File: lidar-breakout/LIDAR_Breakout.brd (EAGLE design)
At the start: 36.5 x 88 mm, 82 parts

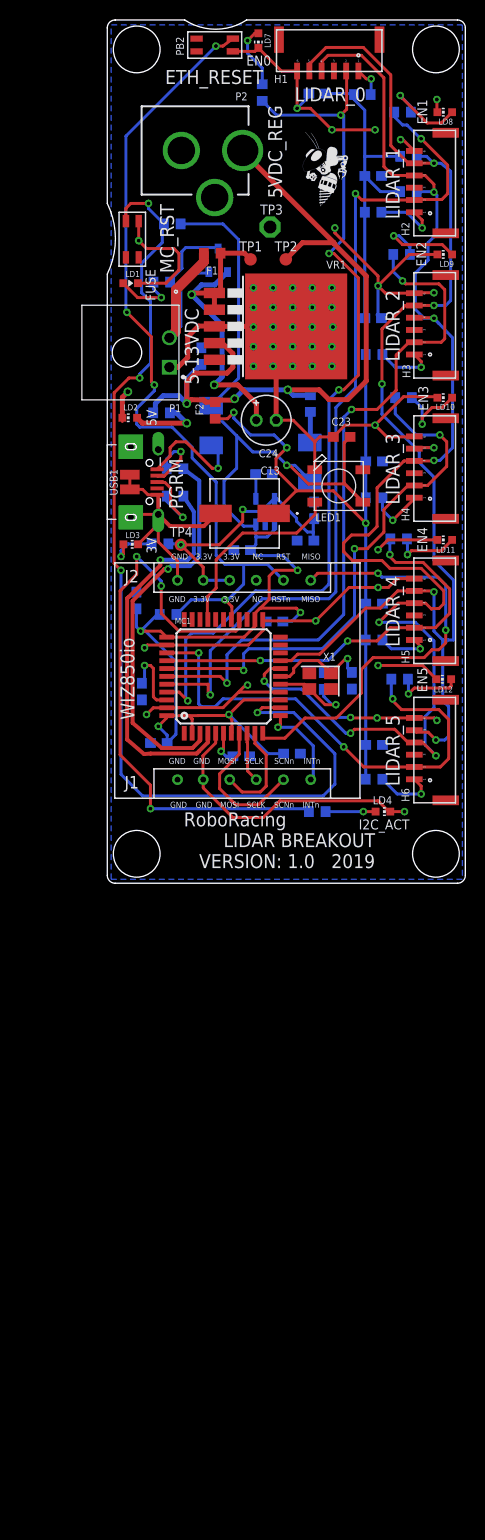
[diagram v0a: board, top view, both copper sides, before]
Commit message: Updated several packages, finished parts list.
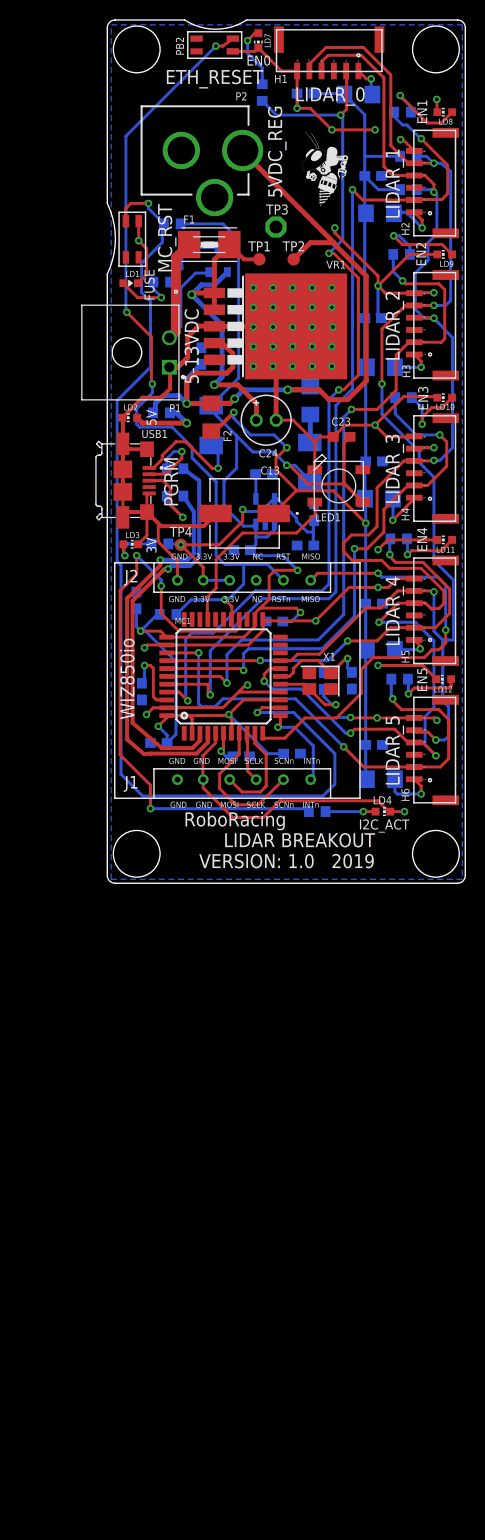
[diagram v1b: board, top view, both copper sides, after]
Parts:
- C3, C4: value 22 pF -> 18 pF
- F1: device RoboJackets-Fuses:F0603 -> adafruit:1812
- F2, F3, F4, F5, F6, F7, F8, F9: device RoboJackets-Fuses:F0603 -> adafruit:R1206
- USB1: value (none) -> 1981584-1; device microbuilder:4UCONN_20329 -> 1981584-1:TE_1981584-1
- moved USB1 2.71 mm to (1.59, 41.0)
- moved F6 1.48 mm to (27.9, 52.6), turned to 180 degrees
- moved F8 1.22 mm to (27.9, 23.8), turned to 180 degrees
- moved C10 1.20 mm to (20.2, 80.5)
- moved F1 0.92 mm to (10.4, 65.1)
- moved TP1 0.90 mm to (15.5, 63.6)
- moved F2 0.81 mm to (10.6, 47.5), turned to 270 degrees
- moved TP2 0.80 mm to (19.0, 63.6)
- moved F5 0.71 mm to (27.8, 68.3), turned to 180 degrees
- moved F9 0.70 mm to (27.9, 10.6), turned to 180 degrees
- moved TP3 0.60 mm to (17.2, 66.9)
- moved F7 0.51 mm to (27.7, 39.2), turned to 180 degrees
- moved C6 0.50 mm to (20.2, 34.4)
- moved F4 0.40 mm to (25.6, 80.4), turned to 180 degrees
- moved F3 0.30 mm to (20.7, 49.2), turned to 270 degrees
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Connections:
- net 5VREG: now also F2.1, F3.1; no longer F2.2, F3.2
- net GND: now also USB1.10, USB1.11, USB1.5, USB1.6, USB1.7, USB1.8, USB1.9; no longer USB1.BASE@1, USB1.BASE@2, USB1.GND, USB1.SPRT@1, USB1.SPRT@2, USB1.SPRT@3, USB1.SPRT@4
- net N$1: now also USB1.1; no longer USB1.VBUS
- net N$23: now also USB1.3; no longer USB1.D+
- net N$7: now also F3.2; no longer F3.1
- net N$8: now also USB1.2; no longer USB1.D-
- net VCC_1: now also F2.2, F4.1, F5.1, F6.1, F7.1, F8.1, F9.1; no longer F2.1, F4.2, F5.2, F6.2, F7.2, F8.2, F9.2
- net VCC_LDR0: now also F4.2; no longer F4.1
- net VCC_LDR1: now also F5.2; no longer F5.1
- net VCC_LDR2: now also F6.2; no longer F6.1
- net VCC_LDR3: now also F7.2; no longer F7.1
- net VCC_LDR4: now also F8.2; no longer F8.1
- net VCC_LDR5: now also F9.2; no longer F9.1
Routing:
- net GND: track 242.9 -> 254.0 mm, vias 47 -> 46
- net VCC_1: track 107.9 -> 110.1 mm
- net VCC_LDR2: track 6.08 -> 4.27 mm
- net VCC_LDR4: track 5.37 -> 3.77 mm
- net VIN: track 34.3 -> 35.5 mm
- net VCC_LDR1: track 6.74 -> 5.51 mm
- net 5VREG: track 78.0 -> 76.9 mm
- net RST_MC: track 105.0 -> 104.1 mm, vias 4 -> 2
- net N$23: track 7.97 -> 8.85 mm
- net N$8: track 6.70 -> 7.54 mm
- net LDR1_EN: track 87.4 -> 88.2 mm
- net VCC_LDR5: track 6.36 -> 5.83 mm
- net VCC_LDR3: track 5.95 -> 5.42 mm

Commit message: Fixed DRC
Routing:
- net GND: track 254.0 -> 249.3 mm
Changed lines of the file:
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@@
 <drawing>
 <settings>
-<setting alwaysvectorfont="yes"/>
+<setting alwaysvectorfont="no"/>
 <setting verticaltext="up"/>
 </settings>
@@
 <layer number="14" name="Route14" color="22" fill="1" visible="no" active="no"/>
 <layer number="15" name="Route15" color="23" fill="1" visible="no" active="no"/>
-<layer number="16" name="Bottom" color="1" fill="1" visible="no" active="yes"/>
+<layer number="16" name="Bottom" color="1" fill="1" visible="yes" active="yes"/>
 <layer number="17" name="Pads" color="2" fill="1" visible="yes" active="yes"/>
 <layer number="18" name="Vias" color="2" fill="1" visible="yes" active="yes"/>
@@
 <contactref element="VR1" pad="6"/>
 <contactref element="TP3" pad="TP"/>
-<wire x1="10.7848" y1="56.9" x2="10.9208" y2="56.764" width="0.2032" layer="1"/>
 <via x="18.9" y="56.7" extent="1-16" drill="0.381"/>
 <wire x1="19.152" y1="56.664" x2="15.7" y2="56.664" width="0.3048" layer="1"/>
@@
 <wire x1="12.8" y1="84.8" x2="15.05" y2="84.8" width="0.3048" layer="1"/>
 <wire x1="15.05" y1="84.8" x2="15.4" y2="85.15" width="0.3048" layer="1"/>
-<wire x1="10.9568" y1="56.8" x2="10.9208" y2="56.764" width="0.508" layer="1"/>
 <wire x1="10.9208" y1="56.764" x2="15.6" y2="56.764" width="0.508" layer="1"/>
 <wire x1="9.75" y1="13" x2="9.75" y2="10.592315625" width="0.3048" layer="1"/>
 <wire x1="9.77831875" y1="10.563996875" x2="9.75" y2="10.592315625" width="0.3048" layer="1"/>
 <wire x1="7.15831875" y1="30.883996875" x2="7.15831875" y2="32.84168125" width="0.3048" layer="1"/>
-<wire x1="5.2" y1="34.8" x2="5.2" y2="36.4" width="0.3048" layer="1"/>
-<wire x1="7.15831875" y1="32.84168125" x2="5.2" y2="34.8" width="0.3048" layer="1"/>
 <wire x1="11.0909" y1="37.65" x2="11.0409" y2="37.7" width="0.3048" layer="1"/>
-<wire x1="19.4" y1="52.2" x2="18.9" y2="52.7" width="0.3048" layer="1"/>
 <via x="22.9" y="76.8" extent="1-16" drill="0.381"/>
 <via x="27.3" y="76.8" extent="1-16" drill="0.381"/>
@@
 <wire x1="24.8" y1="16.85" x2="24.8" y2="16.9" width="0.3048" layer="1"/>
 <via x="24.8" y="16.9" extent="1-16" drill="0.381"/>
-<wire x1="24.8" y1="16.9" x2="23.366" y2="16.9" width="0.3048" layer="16"/>
 <contactref element="P2" pad="GNDBREAK"/>
 <contactref element="C24" pad="-"/>
@@
 <wire x1="15.9" y1="26.8" x2="15.9175" y2="26.8175" width="0.3048" layer="1"/>
 <wire x1="11.0909" y1="37.65" x2="9.8409" y2="36.4" width="0.4064" layer="1"/>
-<wire x1="1.536" y1="47.064" x2="1.536" y2="47.45" width="0.3048" layer="1"/>
 <wire x1="10.9208" y1="56.764" x2="10.8848" y2="56.8" width="0.508" layer="1"/>
 <wire x1="10.8848" y1="56.8" x2="9.3" y2="56.8" width="0.508" layer="1"/>
@@
 <wire x1="4.045" y1="44.24" x2="2.4" y2="44.24" width="0.4064" layer="1"/>
 <wire x1="2.4" y1="44.24" x2="1.555" y2="44.24" width="0.4064" layer="1"/>
-<wire x1="1.755" y1="44.04" x2="1.555" y2="44.24" width="0.4064" layer="1"/>
 <wire x1="4.045" y1="37.84" x2="1.935" y2="37.84" width="0.4064" layer="1"/>
-<wire x1="1.935" y1="37.84" x2="1.495" y2="37.4" width="0.4064" layer="1"/>
 <wire x1="5.485" y1="36.4" x2="4.045" y2="37.84" width="0.4064" layer="1"/>
 <wire x1="9.8409" y1="36.4" x2="5.485" y2="36.4" width="0.4064" layer="1"/>
@@
 <wire x1="6.4" y1="50.4" x2="6.4" y2="52.527" width="0.4064" layer="1"/>
 <wire x1="6.4" y1="52.527" x2="6.327" y2="52.6" width="0.4064" layer="1"/>
-<wire x1="1.595" y1="44.79" x2="1.595" y2="43.9" width="0.3048" layer="1"/>
 <wire x1="1.595" y1="44.79" x2="2.145" y2="44.24" width="0.3048" layer="1"/>
 <wire x1="2.145" y1="44.24" x2="2.4" y2="44.24" width="0.3048" layer="1"/>
@@
 <wire x1="3.128" y1="61.169" x2="4" y2="62.041" width="0.3048" layer="1"/>
 <wire x1="4" y1="62.041" x2="4" y2="64.7" width="0.3048" layer="1"/>
+<wire x1="4.54396875" y1="35.45603125" x2="4.045" y2="35.45603125" width="0.3048" layer="1"/>
+<wire x1="7.15831875" y1="32.84168125" x2="4.54396875" y2="35.45603125" width="0.3048" layer="1"/>
 </signal>
 <signal name="RST_MC">

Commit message: Reran cam
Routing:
- net GND: track 249.3 -> 247.2 mm
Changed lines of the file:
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@@
 <contactref element="USB1" pad="10"/>
 <wire x1="1.595" y1="42.19" x2="1.595" y2="39.89" width="0.4064" layer="1"/>
-<wire x1="1.595" y1="43.9" x2="1.595" y2="42.19" width="0.4064" layer="1"/>
-<wire x1="4.045" y1="44.24" x2="2.4" y2="44.24" width="0.4064" layer="1"/>
-<wire x1="2.4" y1="44.24" x2="1.555" y2="44.24" width="0.4064" layer="1"/>
-<wire x1="4.045" y1="37.84" x2="1.935" y2="37.84" width="0.4064" layer="1"/>
 <wire x1="5.485" y1="36.4" x2="4.045" y2="37.84" width="0.4064" layer="1"/>
 <wire x1="9.8409" y1="36.4" x2="5.485" y2="36.4" width="0.4064" layer="1"/>
@@
 <wire x1="6.4" y1="50.4" x2="6.4" y2="52.527" width="0.4064" layer="1"/>
 <wire x1="6.4" y1="52.527" x2="6.327" y2="52.6" width="0.4064" layer="1"/>
-<wire x1="1.595" y1="44.79" x2="2.145" y2="44.24" width="0.3048" layer="1"/>
-<wire x1="2.145" y1="44.24" x2="2.4" y2="44.24" width="0.3048" layer="1"/>
 <wire x1="1.595" y1="39.89" x2="1.595" y2="37.29" width="0.3048" layer="1"/>
-<wire x1="1.595" y1="37.29" x2="2.145" y2="37.84" width="0.3048" layer="1"/>
-<wire x1="2.145" y1="37.84" x2="4.045" y2="37.84" width="0.3048" layer="1"/>
 <wire x1="3.128" y1="61.169" x2="4" y2="62.041" width="0.3048" layer="1"/>
 <wire x1="4" y1="62.041" x2="4" y2="64.7" width="0.3048" layer="1"/>
 <wire x1="4.54396875" y1="35.45603125" x2="4.045" y2="35.45603125" width="0.3048" layer="1"/>
 <wire x1="7.15831875" y1="32.84168125" x2="4.54396875" y2="35.45603125" width="0.3048" layer="1"/>
+<wire x1="4.045" y1="44.24" x2="2.145" y2="44.24" width="0.4064" layer="1"/>
+<wire x1="2.145" y1="44.24" x2="1.595" y2="44.79" width="0.4064" layer="1"/>
+<wire x1="1.595" y1="44.79" x2="1.595" y2="42.19" width="0.4064" layer="1"/>
+<wire x1="1.595" y1="37.29" x2="2.145" y2="37.84" width="0.4064" layer="1"/>
+<wire x1="2.145" y1="37.84" x2="4.045" y2="37.84" width="0.4064" layer="1"/>
 </signal>
 <signal name="RST_MC">

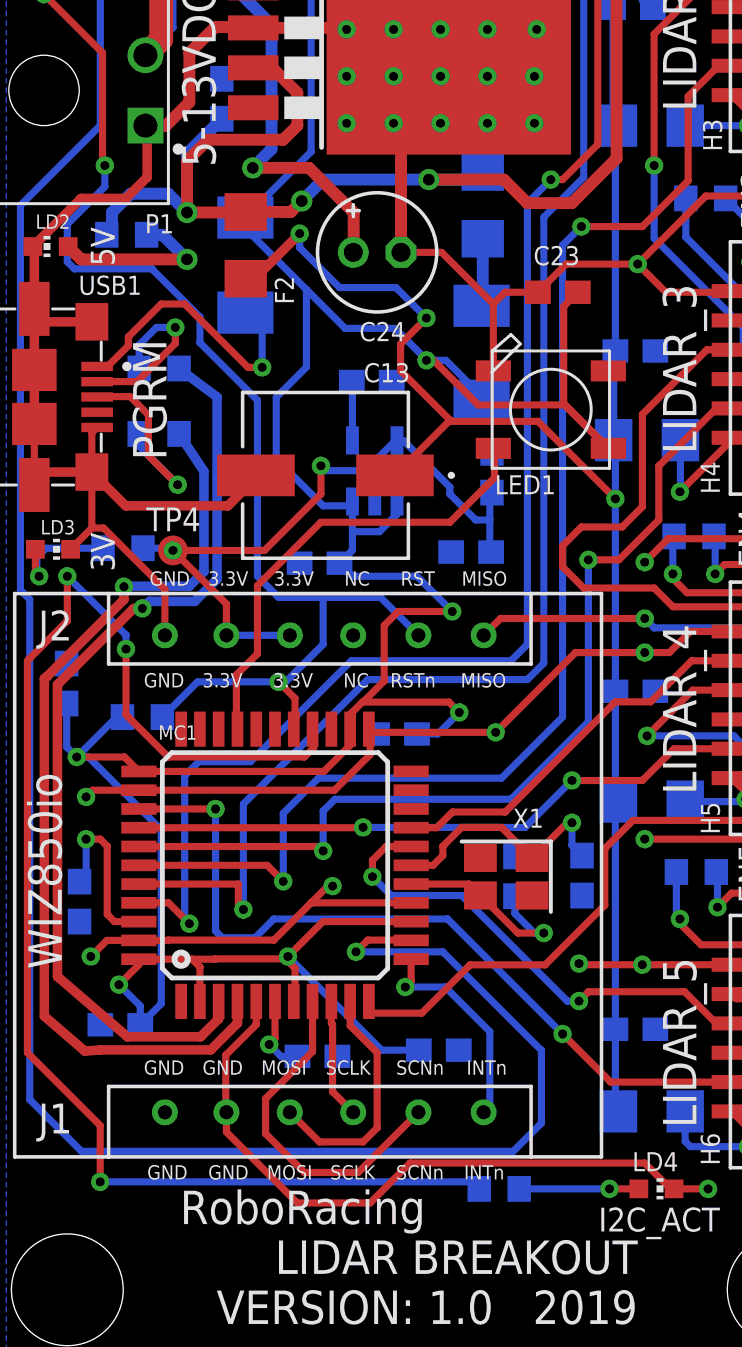
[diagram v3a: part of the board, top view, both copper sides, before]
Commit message: Updated Wiz850io footprint
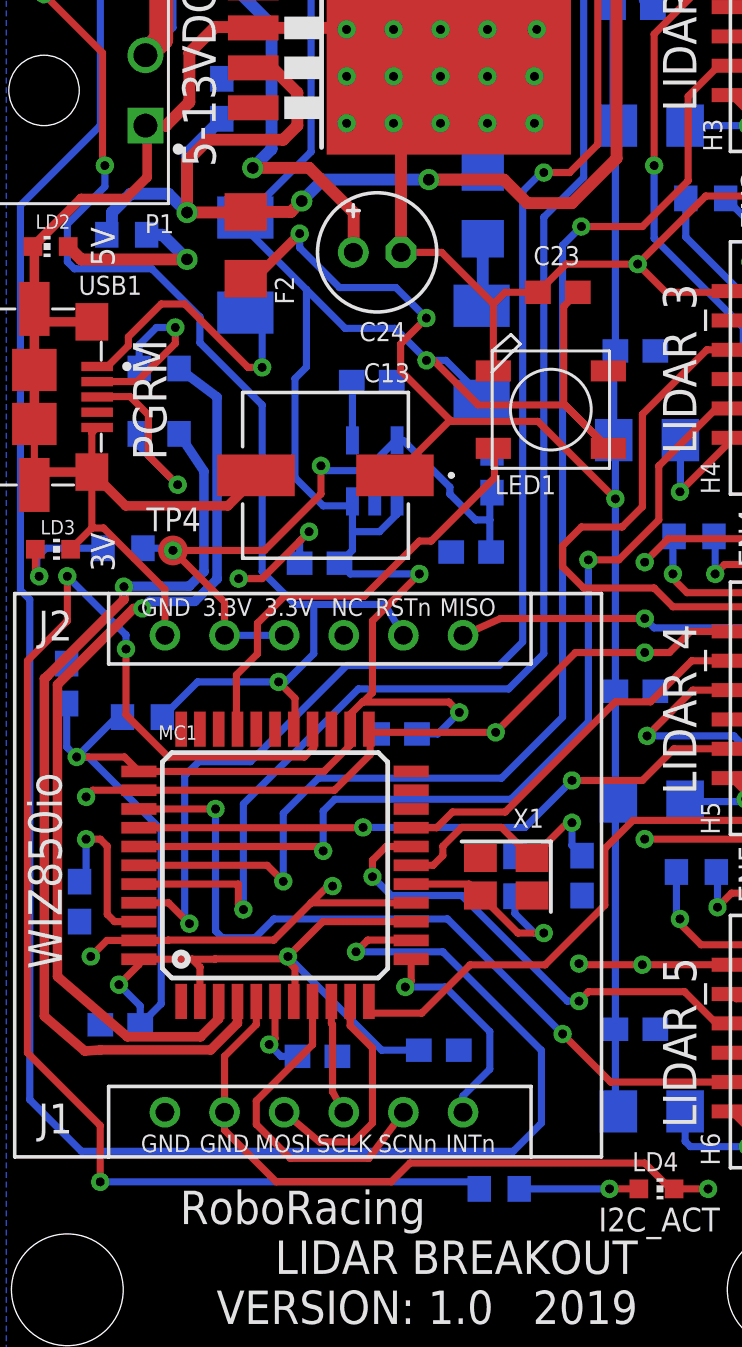
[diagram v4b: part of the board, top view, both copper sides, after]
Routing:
- net GND: track 247.2 -> 251.9 mm, vias 46 -> 48
- net VCC_2: track 151.9 -> 148.8 mm
- net RST_ETH: track 85.1 -> 84.0 mm
- net STATUS_PWM: track 19.8 -> 18.8 mm
- net MISO_ETH: track 45.0 -> 45.8 mm
- net SCNN_ETH: track 14.7 -> 14.1 mm
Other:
- board text removed: "3.3V"
- board text removed: "GND"
- board text removed: "INTn"
- board text removed: "MISO"
- board text removed: "MOSI"
- board text removed: "NC"
- board text removed: "RST"
- board text removed: "SCLK"
- board text removed: "SCNn"

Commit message: Updated values for crystal caps
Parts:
- C3, C4: value 18 pF -> 9 pF
- X1: value (none) -> TSX-3225 16.0000MF18X-AC0
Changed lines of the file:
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@@
 <drawing>
 <settings>
-<setting alwaysvectorfont="yes"/>
+<setting alwaysvectorfont="no"/>
 <setting verticaltext="up"/>
 </settings>
@@
 <attribute name="VALUE" x="7.679" y="53.108" size="1.27" layer="28" rot="MR90"/>
 </element>
-<element name="C3" library="resistor" library_urn="urn:adsk.eagle:library:348" package="C0603" package3d_urn="urn:adsk.eagle:package:26138/1" value="18 pF" x="24.931" y="20.646" smashed="yes" rot="MR270">
+<element name="C3" library="resistor" library_urn="urn:adsk.eagle:library:348" package="C0603" package3d_urn="urn:adsk.eagle:package:26138/1" value="9 pF" x="24.931" y="20.646" smashed="yes" rot="MR270">
 <attribute name="NAME" x="20.796" y="21.081" size="0.8128" layer="26" font="vector" rot="MR270"/>
 <attribute name="VALUE" x="26.836" y="21.281" size="1.27" layer="28" rot="MR270"/>
@@
 <attribute name="VALUE" x="19.187" y="37.177" size="1.27" layer="28" rot="MR90"/>
 </element>
-<element name="C4" library="resistor" library_urn="urn:adsk.eagle:library:348" package="C0603" package3d_urn="urn:adsk.eagle:package:26138/1" value="18 pF" x="22.069" y="20.618" smashed="yes" rot="MR90">
+<element name="C4" library="resistor" library_urn="urn:adsk.eagle:library:348" package="C0603" package3d_urn="urn:adsk.eagle:package:26138/1" value="9 pF" x="22.069" y="20.618" smashed="yes" rot="MR90">
 <attribute name="NAME" x="26.104" y="20.183" size="0.8128" layer="26" font="vector" rot="MR90"/>
 <attribute name="VALUE" x="20.164" y="19.983" size="1.27" layer="28" rot="MR90"/>
@@
 </element>
 <element name="ETH1" library="WIZ850io" package="WIZ850IO" value="WIZ850IO" x="0.75831875" y="8.663996875" smashed="yes"/>
-<element name="X1" library="RoboJackets-FreqGen" package="XTAL-3.2X2.5" value="" x="21.7" y="20.6" smashed="yes" rot="R180">
+<element name="X1" library="RoboJackets-FreqGen" package="XTAL-3.2X2.5" value="TSX-3225 16.0000MF18X-AC0 " x="21.7" y="20.6" smashed="yes" rot="R180">
 <attribute name="NAME" x="23.3" y="23.5" size="0.8128" layer="25" font="vector" rot="R180"/>
 </element>

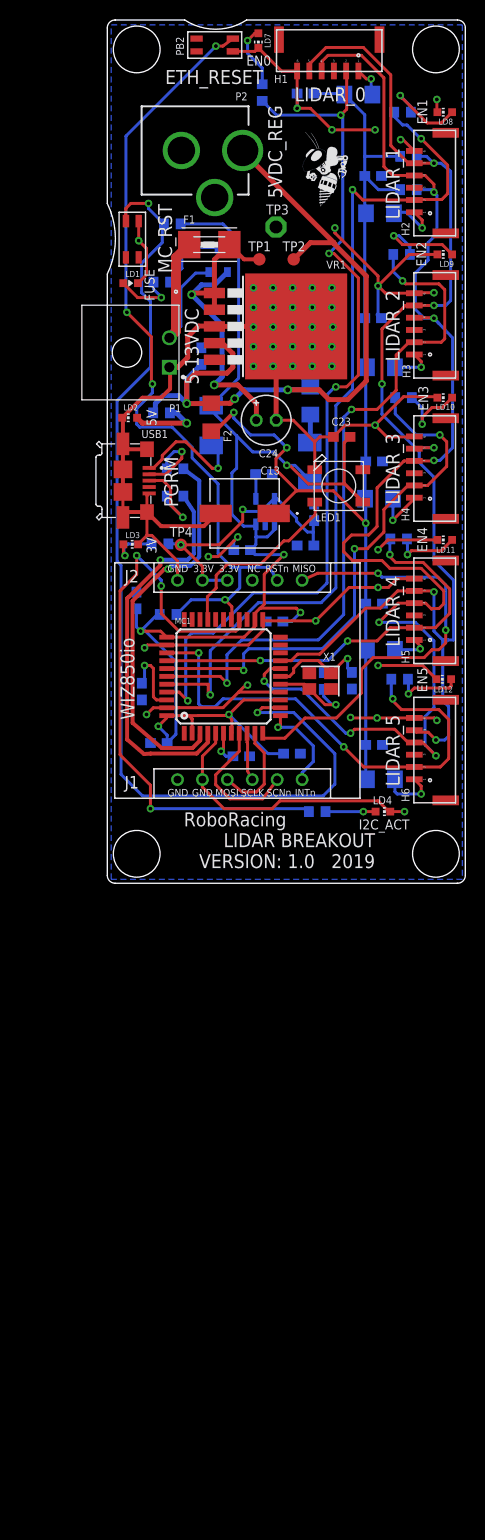
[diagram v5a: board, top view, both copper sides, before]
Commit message: Fixed R22 Package Size, Added Error Leds
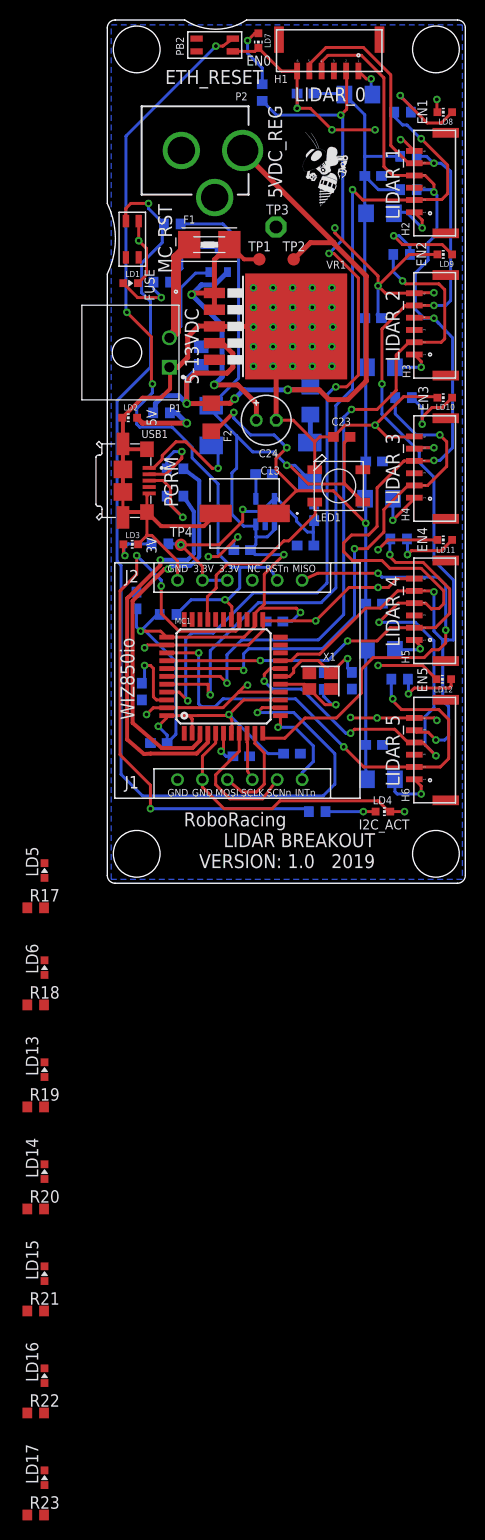
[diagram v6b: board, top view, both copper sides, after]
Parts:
- added LD13, LD14, LD15, LD16, LD17, LD5, LD6: RED, RoboJackets-LEDs:CHIP-LED0603
- added R17, R18, R19, R20, R21, R22, R23: 1 kΩ, rcl:R0603
- C22: device resistor:C0603 -> rcl:C0805
- P1: value (none) -> MOLEX 0436500200
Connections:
- new net COMM_ERR: R17.1
- new net LDR2_ERR: R19.1
- new net LDR6_ERR: R18.1, R20.1, R21.1, R22.1, R23.1
- new net N$10: LD6.A, R18.2
- new net N$11: LD13.A, R19.2
- new net N$12: LD14.A, R20.2
- new net N$13: LD15.A, R21.2
- new net N$14: LD16.A, R22.2
- new net N$15: LD17.A, R23.2
- new net N$9: LD5.A, R17.2
- net GND: now also LD13.C, LD14.C, LD15.C, LD16.C, LD17.C, LD5.C, LD6.C
